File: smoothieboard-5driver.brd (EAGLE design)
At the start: 105.1 x 105.1 mm, 234 parts, among them IC1 LPC1769, IC10 LM1117-3.3V, IC11 78L12F, IC2 A4982, IC3 A4982, IC4 MCP44X1, IC5 A4982, IC6 A4982, J10 POWER_JACKSMD, Q1 BSL207SP, Q2 12MHz, Q3 25MHz, Q6 AOT240L, Q7 AOT240L, Q8 ZXMN4A06GTA, Q9 ZXMN4A06GTA, U1 USD-SOCKETNEW, X14 USBPTH

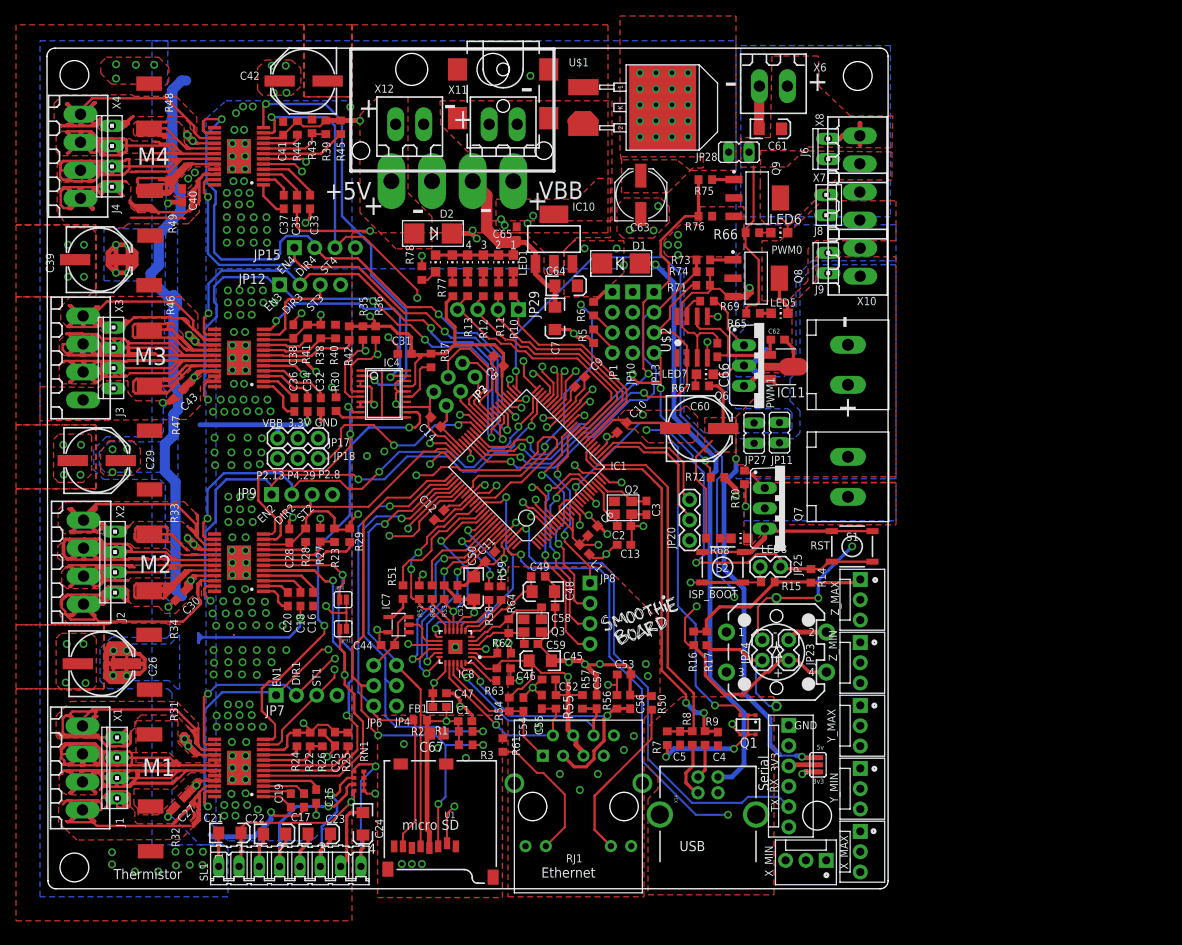
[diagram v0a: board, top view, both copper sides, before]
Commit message: Added 5th driver, 2nd digipot. Still lots of layout work to do
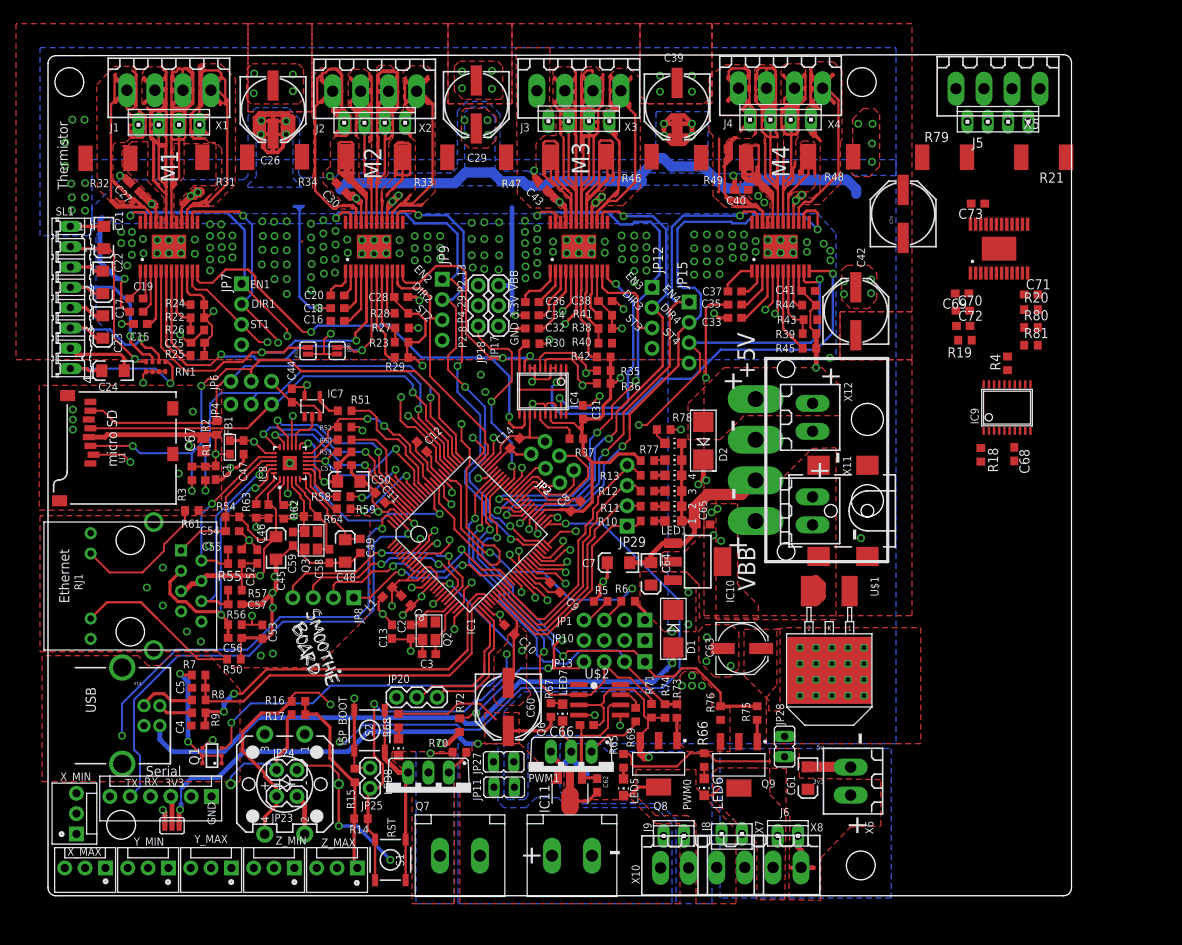
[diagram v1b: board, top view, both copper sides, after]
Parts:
- added C68, C69, C70, C71, C73: .1uF, rcl:C0603
- added C72: .22uF, rcl:C0603
- added C74: 100uF, SparkFun:PANASONIC_E
- added IC12: A4982, A4982:ETSSOP24
- added IC9: MCP44X1, Geos:TSSOP20
- added J5: (no value), con-amp:10X04MTA
- added R18: 33K, resistor:R0603
- added R19, R20, R81: 10K, resistor:R0603
- added R21, R79: 0.05R, SparkFun:R2512
- added R4: 100K, resistor:R0603
- added R80: NP, resistor:R0603
- added X5: (no value), con-weidmueller-sl35:180G-4
- moved JP14 94.5 mm to (7.18, 2.60), turned to 180 degrees
- moved JP26 93.8 mm to (3.56, 6.86), turned to 90 degrees
- moved X8 90.2 mm to (92.4, 2.67), turned to 180 degrees
- moved X4 87.9 mm to (91.6, 100.1), turned to 180 degrees
- moved X6 87.4 mm to (100.3, 13.5), turned to 90 degrees
- moved JP16 87.4 mm to (15.0, 2.60), turned to 180 degrees
- moved J6 86.0 mm to (92.5, 6.62), turned to 0 degrees
- moved R48 85.5 mm to (97.9, 91.5), turned to 180 degrees
- moved X1 85.4 mm to (15.1, 99.8), turned to 180 degrees
- moved X7 84.2 mm to (85.3, 2.67), turned to 180 degrees
- moved R32 84.0 mm to (7.49, 91.3), turned to 0 degrees
- moved J4 83.7 mm to (91.6, 96.1), turned to 0 degrees
- moved C61 81.3 mm to (95.0, 13.8), turned to 270 degrees
- moved JP19 81.2 mm to (22.9, 2.60), turned to 180 degrees
- moved SJ1 81.1 mm to (15.5, 7.89), turned to 0 degrees
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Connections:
- new net DIR5: IC12.P14
- new net EN5: IC12.P23
- new net N$29: IC9.15, R4.1
- new net N$56: IC9.1, IC9.10, IC9.11, IC9.20, R18.1
- new net N$58: C69.2, IC12.P01
- new net N$59: C69.1, IC12.P02
- new net N$64: C70.2, IC12.P03
- new net N$65: IC12.P17, R21.2
- new net N$66: IC12.P20, R79.2
- new net N$70: IC12.P18, J5.2, X5.2
- new net N$71: IC12.P15, J5.1, X5.1
- new net N$72: IC12.P19, J5.3, X5.3
- new net N$76: IC12.P22, J5.4, X5.4
- new net N$79: IC12.P08, R19.1, R80.1
- new net N$83: C72.2, IC12.P04
- new net N$89: IC12.P09, R20.1
- new net N$95: IC12.P07, R81.1
- new net PW5: IC12.P12, IC9.12
- new net STEP5: IC12.P11
- net 3.3V: now also C68.2, C71.1, IC12.P10, IC9.17, IC9.4, R18.2, R20.2, R4.2, R80.2, R81.2
- net GND: now also C68.1, C71.2, C72.1, C73.2, C74.-, IC12.EPAD, IC12.P13, IC12.P24, IC9.13, IC9.16, IC9.18, IC9.3, IC9.7, IC9.8, R19.2, R21.1, R79.1
- net MS1: now also IC12.P05
- net MS2: now also IC12.P06
- net POT_SCL: now also IC9.5
- net POT_SDA: now also IC9.6
- net VBB: now also C70.1, C73.1, C74.+, IC12.P16, IC12.P21
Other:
- board size 105.1 x 105.1 mm -> 127.9 x 105.1 mm

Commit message: shifted power connectors, lots of rearranging, still more to do
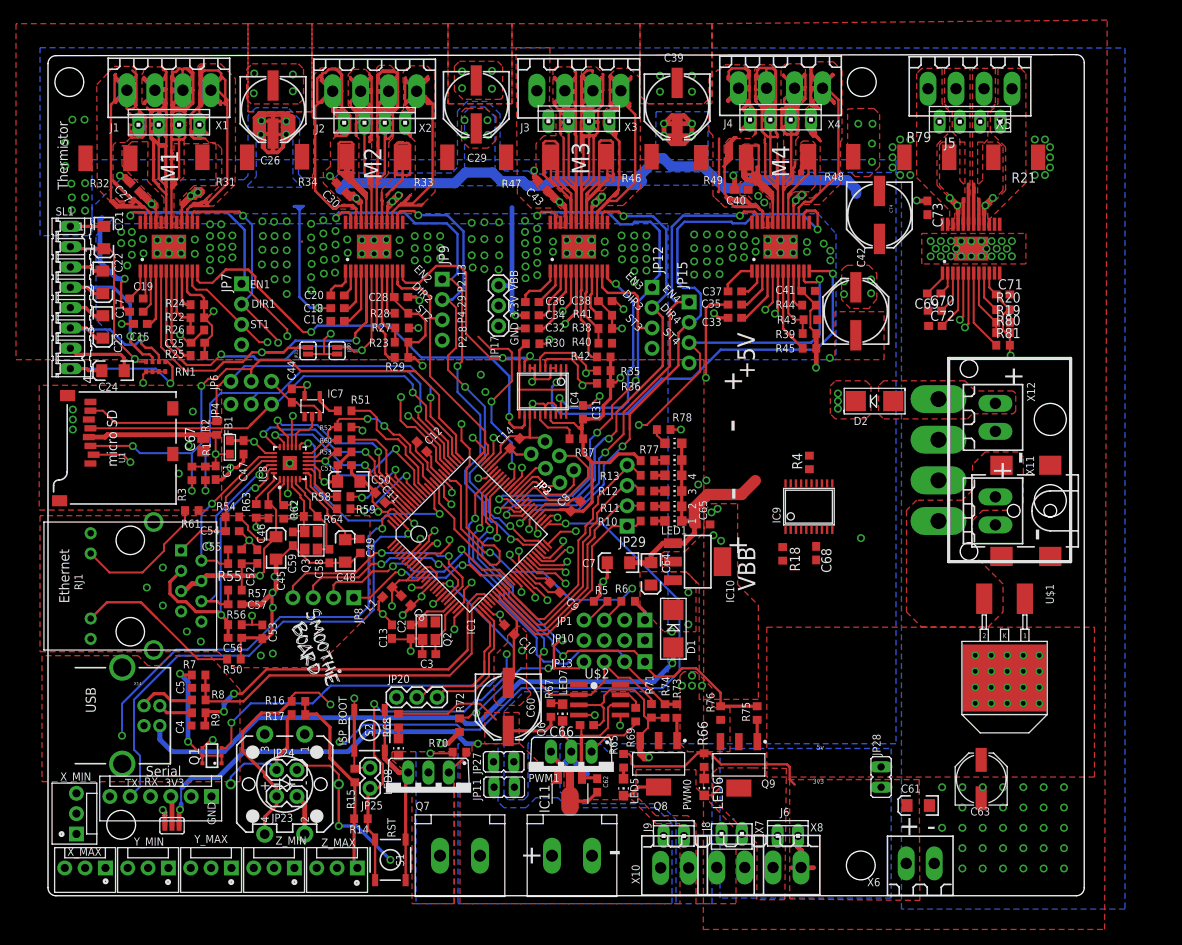
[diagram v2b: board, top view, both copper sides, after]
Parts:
- removed JP18: (no value), SparkFun:1X03
- moved C63 34.1 mm to (116.6, 13.7), turned to 90 degrees
- moved R4 27.7 mm to (95.2, 53.3)
- moved C68 27.7 mm to (96.0, 42.0)
- moved IC9 27.7 mm to (95.1, 47.8)
- moved R18 27.7 mm to (91.8, 41.9)
- moved J10 22.9 mm to (125.3, 47.2)
- moved POWER 22.9 mm to (112.6, 43.4)
- moved X11 22.9 mm to (118.4, 47.2)
- moved X12 22.9 mm to (118.4, 58.9)
- moved D2 22.0 mm to (103.3, 61.0), turned to 0 degrees
- moved U$1 21.9 mm to (125.9, 38.8)
- moved C61 14.2 mm to (108.8, 10.4), turned to 180 degrees
- moved X6 13.5 mm to (109.0, 3.17), turned to 0 degrees
- moved JP28 12.7 mm to (104.1, 14.0)
- moved C73 6.34 mm to (109.9, 85.1), turned to 270 degrees
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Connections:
- removed net P2.13: IC1.50, JP18.3
- removed net P2.8: IC1.65, JP18.1
- removed net P4.29: IC1.85, JP18.2
- removed net STEP5: IC12.P11
- new net STP5: IC1.65, IC12.P11
- net DIR5: now also IC1.50
- net EN5: now also IC1.85
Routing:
- net P4.29: track 54.5 -> 0.00 mm, vias 2 -> 0
- net EN5: track 0.00 -> 53.1 mm, vias 0 -> 2
- net P2.13: track 46.3 -> 0.00 mm, vias 2 -> 0
- net DIR5: track 0.00 -> 44.5 mm, vias 0 -> 2
- net 3.3V: track 250.2 -> 291.6 mm, vias 24 -> 25
- net MS1: track 135.9 -> 165.3 mm, vias 4 -> 5
- net MS2: track 137.9 -> 166.3 mm, vias 4 -> 5
- net P2.8: track 25.5 -> 0.00 mm, vias 2 -> 0
- net STP5: track 0.00 -> 24.1 mm, vias 0 -> 2
- net 5V: track 84.8 -> 104.3 mm, vias 6 -> 9
- net N$95: track 0.00 -> 10.2 mm
- net VBB: track 326.9 -> 335.7 mm, vias 54 -> 59
- net N$79: track 0.00 -> 8.34 mm
- net N$83: track 0.00 -> 7.44 mm
- net GND: track 286.4 -> 281.0 mm, vias 233 -> 279
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- added copper zone on layer 1, net N$65
- added copper zone on layer 1, net N$66
- added copper zone on layer 1, net N$70
- added copper zone on layer 1, net N$71
- added copper zone on layer 1, net N$72
- added copper zone on layer 1, net N$76
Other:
- board size 127.9 x 105.1 mm -> 129.5 x 105.1 mm

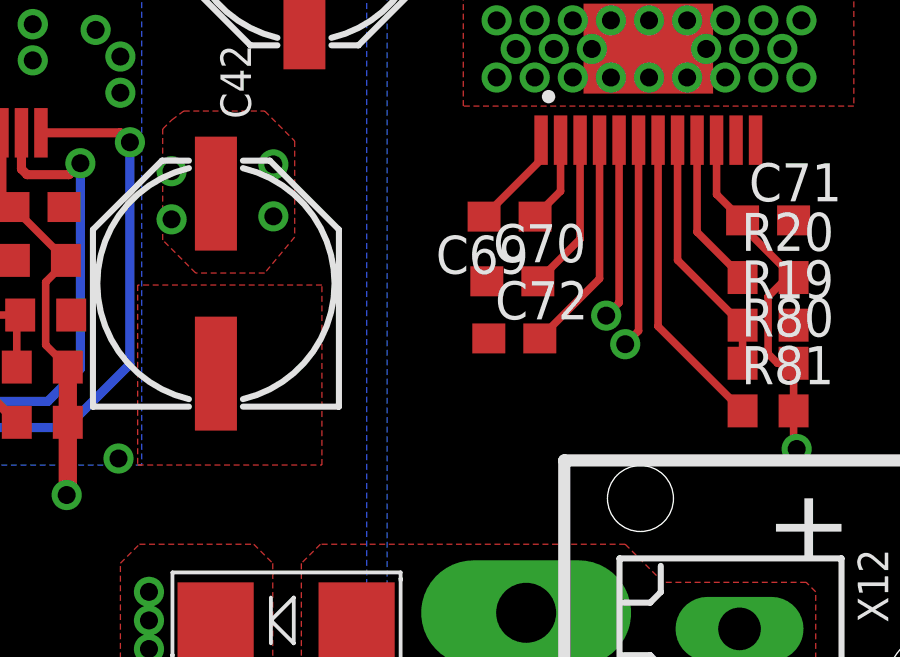
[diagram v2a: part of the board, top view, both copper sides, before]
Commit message: added 1x4 connector for 5th driver en/dir/step signals to match other drivers
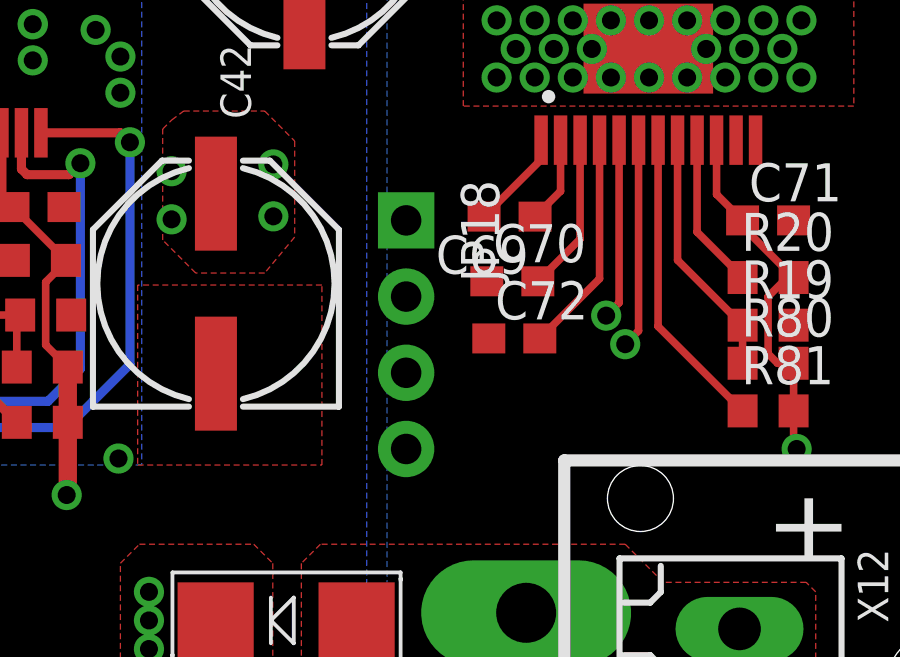
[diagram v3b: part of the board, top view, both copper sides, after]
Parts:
- added JP18: (no value), SparkFun:1X04_NO_SILK
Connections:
- net DIR5: now also JP18.2
- net EN5: now also JP18.1
- net GND: now also JP18.4
- net STP5: now also JP18.3
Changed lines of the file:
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@@
 <element name="R81" library="resistor" package="R0603" value="10K" x="119.38" y="67.945"/>
 <element name="C74" library="SparkFun" package="PANASONIC_E" value="100uF" x="103.925" y="84.23" rot="R270"/>
+<element name="JP18" library="SparkFun" package="1X04_NO_SILK" value="" x="107.315" y="74.295" rot="R270"/>
 </elements>
 <signals>
@@
 <vertex x="109.22" y="78.105"/>
 </polygon>
+<contactref element="JP18" pad="4"/>
 <wire x1="13.6525" y1="79.4385" x2="13.5255" y2="79.248" width="0" layer="19" extent="1-1"/>
 </signal>
@@
 <wire x1="51.689" y1="58.1025" x2="51.689" y2="59.1185" width="0.254" layer="15"/>
 <wire x1="51.689" y1="59.1185" x2="54.6735" y2="62.103" width="0.254" layer="15"/>
-<wire x1="55.753" y1="64.897" x2="112.4625" y2="83.07" width="0" layer="19" extent="1-2"/>
+<contactref element="JP18" pad="1"/>
+<wire x1="107.315" y1="74.295" x2="112.4625" y2="83.07" width="0" layer="19" extent="1-1"/>
+<wire x1="55.753" y1="64.897" x2="107.315" y2="74.295" width="0" layer="19" extent="1-2"/>
 </signal>
 <signal name="STP5">
@@
 <wire x1="55.4355" y1="60.8965" x2="55.4355" y2="58.293" width="0.254" layer="16"/>
 <wire x1="57.9755" y1="55.753" x2="57.9755" y2="52.832" width="0.254" layer="16"/>
-<wire x1="57.9755" y1="67.056" x2="118.3125" y2="76.97" width="0" layer="19" extent="1-1"/>
+<contactref element="JP18" pad="3"/>
+<wire x1="107.315" y1="69.215" x2="118.3125" y2="76.97" width="0" layer="19" extent="1-1"/>
+<wire x1="57.9755" y1="67.056" x2="107.315" y2="69.215" width="0" layer="19" extent="1-1"/>
 </signal>
 <signal name="DIR5">
@@
 <wire x1="54.102" y1="64.262" x2="55.878" y2="64.262" width="0.254" layer="15"/>
 <wire x1="65.9765" y1="44.704" x2="65.9765" y2="46.228" width="0.254" layer="15"/>
-<wire x1="65.9765" y1="46.228" x2="118.3125" y2="83.07" width="0" layer="19" extent="1-15"/>
+<contactref element="JP18" pad="2"/>
+<wire x1="107.315" y1="71.755" x2="118.3125" y2="83.07" width="0" layer="19" extent="1-1"/>
+<wire x1="65.9765" y1="46.228" x2="107.315" y2="71.755" width="0" layer="19" extent="1-15"/>
 </signal>
 <signal name="PW5">

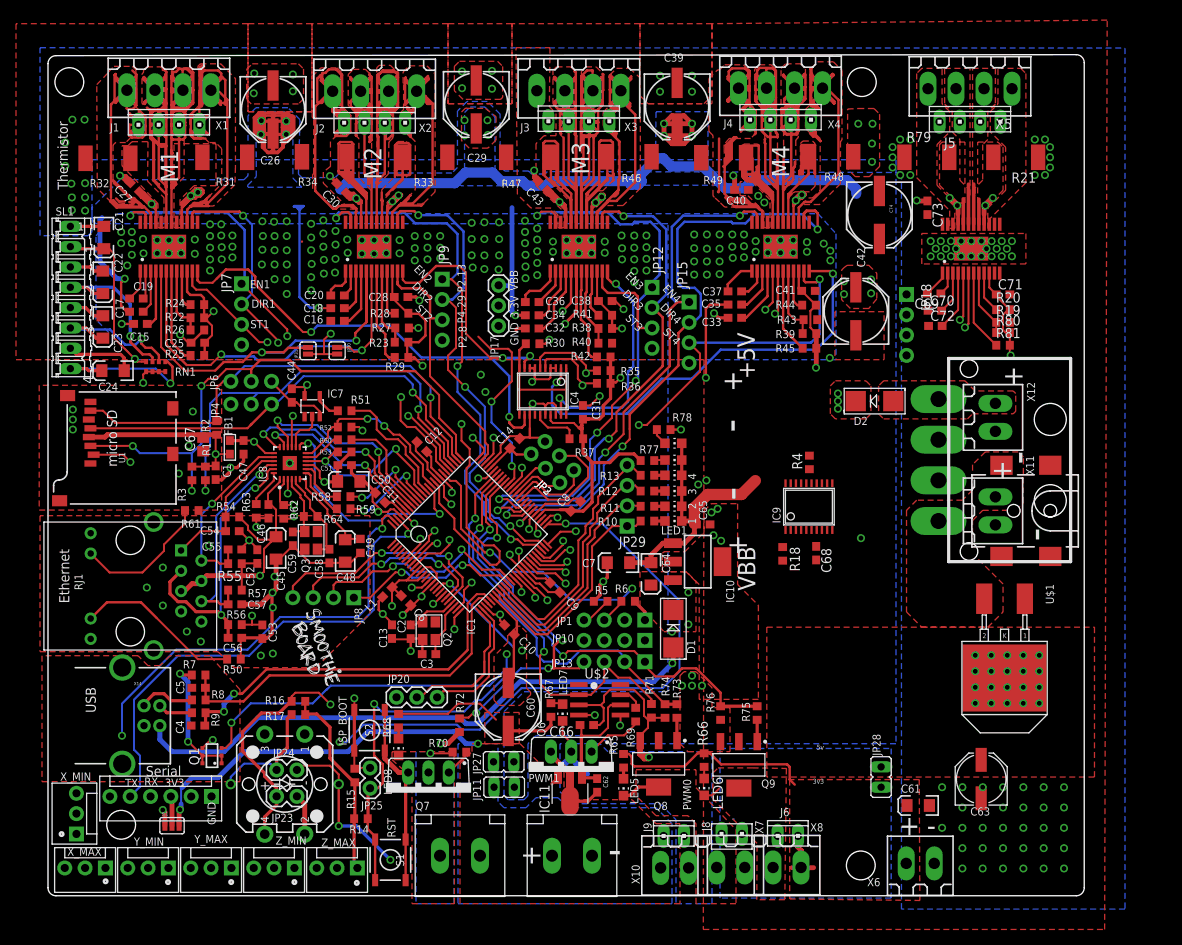
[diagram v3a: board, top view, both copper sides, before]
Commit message: Routing complete, DRC passes, now time for fine tuning
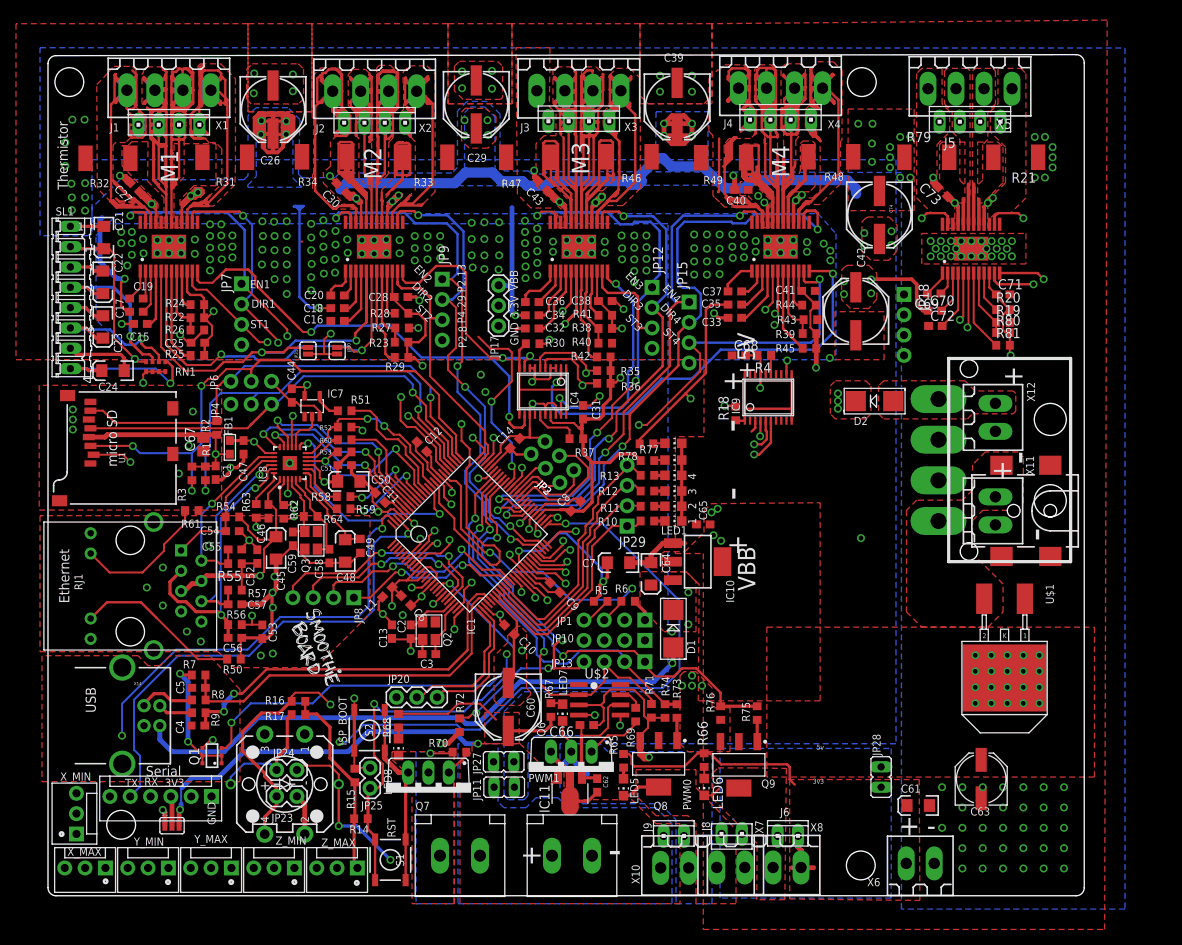
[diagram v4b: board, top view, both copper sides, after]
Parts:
- moved C68 26.5 mm to (86.4, 66.7), turned to 0 degrees
- moved R18 18.5 mm to (86.0, 59.4), turned to 90 degrees
- moved IC9 14.6 mm to (90.0, 61.4)
- moved R4 14.5 mm to (89.5, 66.7), turned to 180 degrees
- moved R78 2.80 mm to (74.8, 55.6), turned to 180 degrees
- moved C73 2.77 mm to (111.8, 87.1), turned to 135 degrees
- moved JP18 0.32 mm to (107.0, 74.3)
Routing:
- net DIR5: track 44.5 -> 134.5 mm, vias 2 -> 4
- net STP5: track 24.1 -> 114.0 mm, vias 2 -> 3
- net EN5: track 53.1 -> 125.7 mm, vias 2 -> 3
- net PW5: track 0.00 -> 46.1 mm, vias 0 -> 2
- net POT_SCL: track 36.5 -> 69.2 mm, vias 2 -> 3
- net POT_SDA: track 40.1 -> 71.0 mm, vias 2 -> 3
- net N$56: track 0.00 -> 18.7 mm
- net GND: track 281.0 -> 265.2 mm, vias 279 -> 300
- net VBB: track 335.7 -> 351.1 mm, vias 59 -> 60
- net N$45: track 24.3 -> 9.23 mm
- net MS2: track 166.3 -> 175.5 mm
- net MS1: track 165.3 -> 174.3 mm
- net 3.3V: track 291.6 -> 300.1 mm, vias 25 -> 28
- net 5V: track 104.3 -> 109.4 mm, vias 9 -> 7
- net N$29: track 0.00 -> 2.35 mm
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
